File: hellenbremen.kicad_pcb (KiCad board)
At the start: 4 copper layers, 102 x 107 mm, 64 parts, among them IC1 TLE9201SG, J2 Conn_01x03_Pin, J3 USB_C_Receptacle_USB2.0_16P, M1 Module-stlink-0.1, M2 Module-power_12and5V-0.2, M3 Module-mega-mcu144-0.6, M4 Module-vr-max9924-0.1, M5 Module-knock-0.2, M6 Module-knock-0.2, Q1 ISL9V3040D3ST, Q2 ISL9V3040D3ST, Q3 DMN6040SK3-13, Q4 DMN6040SK3-13, U1 RNBD451PE-I100, U2 VNLD5160TR-E, U3 VNLD5160TR-E, U4 VNLD5160TR-E, U7 VNLD5160TR-E, U8 VNLD5160TR-E

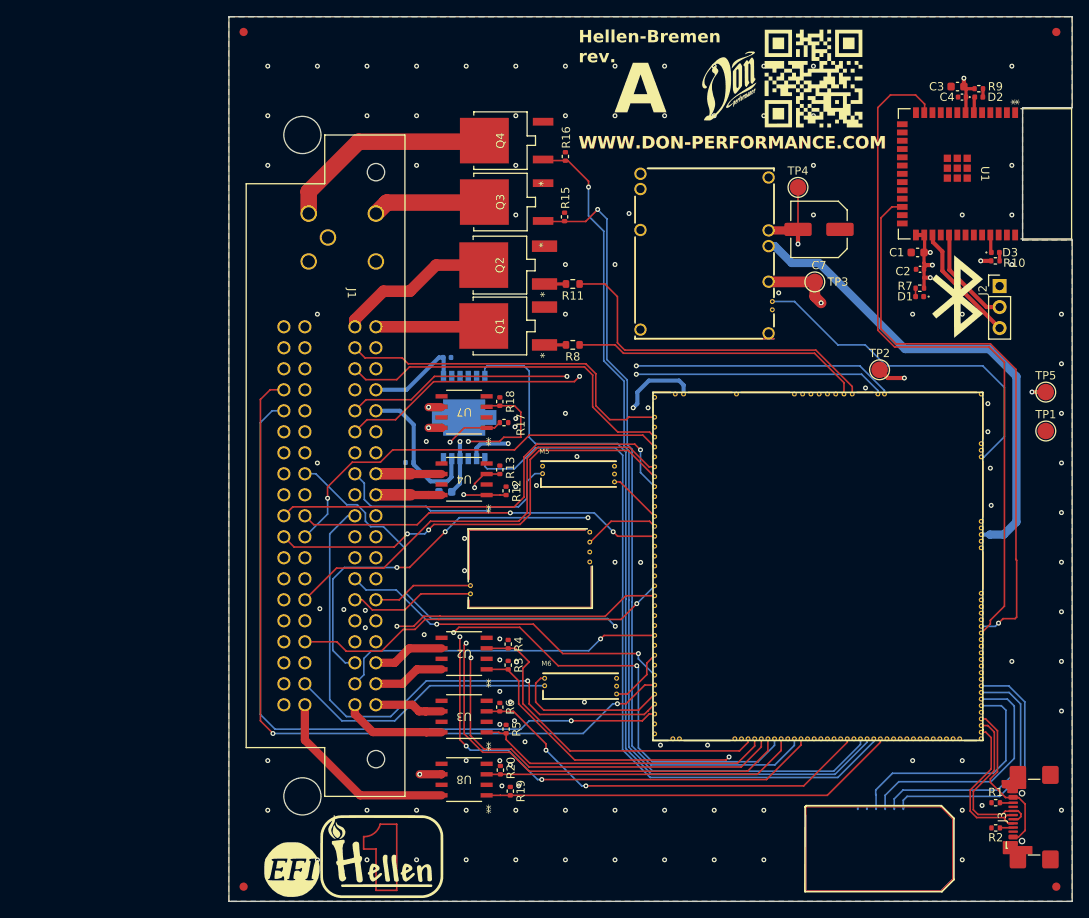
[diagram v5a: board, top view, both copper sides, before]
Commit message: pwm for heaters, minor routing and via changes, teardrops
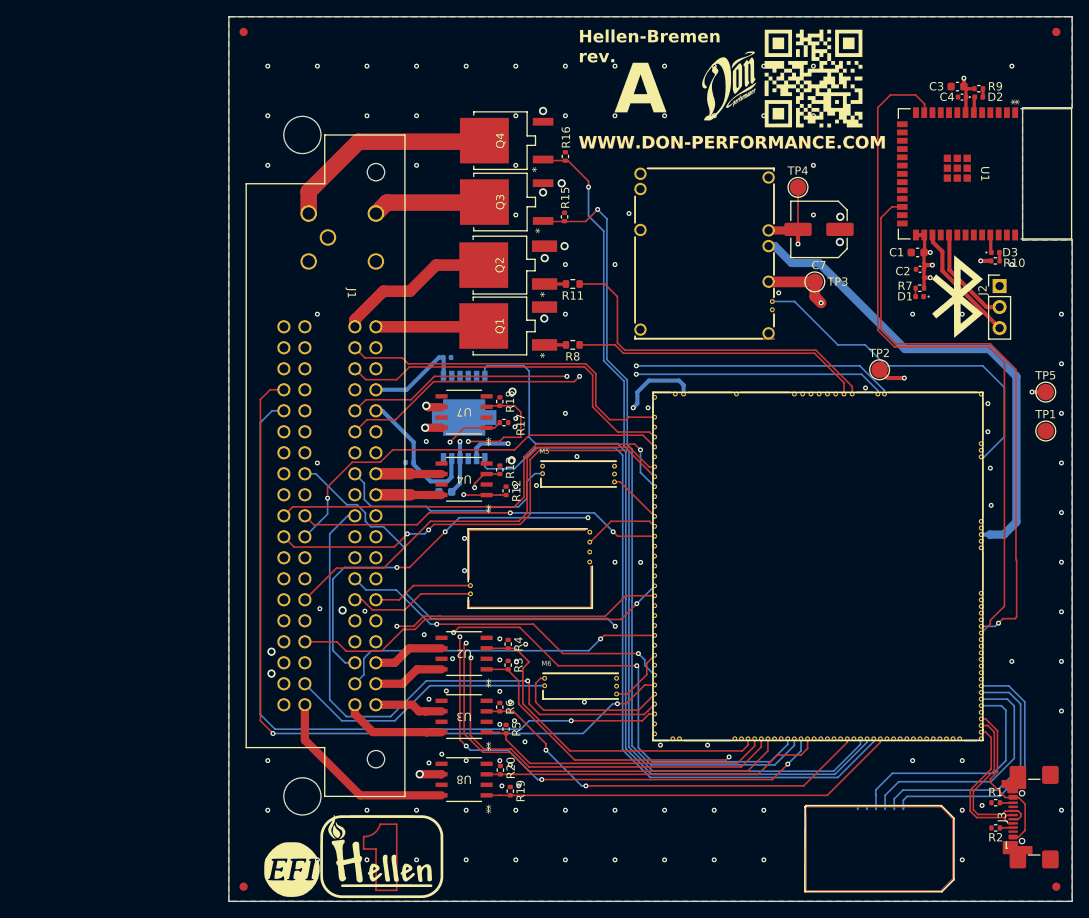
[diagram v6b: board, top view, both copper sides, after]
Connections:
- M3 pad E25: unconnected-(M3-OUT_PWM7-PadE25) -> MCU_FHO2H
- M3 pad E28: unconnected-(M3-OUT_PWM8-PadE28) -> MCU_RHO2H
- M3 pad E29: MCU_FHO2H -> unconnected-(M3-OUT_INJ3-PadE29)
- M3 pad E30: MCU_RHO2H -> unconnected-(M3-OUT_INJ4-PadE30)
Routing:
- net MCU_FHO2H: track 38.2 -> 41.3 mm
- net MCU_RHO2H: track 83.3 -> 84.9 mm
- net ETC_OUT_M: track 18.0 -> 16.8 mm
- net MCU_PCHO2SHTR: track 97.3 -> 97.7 mm, vias 4 -> 5
- net GND: vias 118 -> 132

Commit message: large cap, more silkscreen for big connector
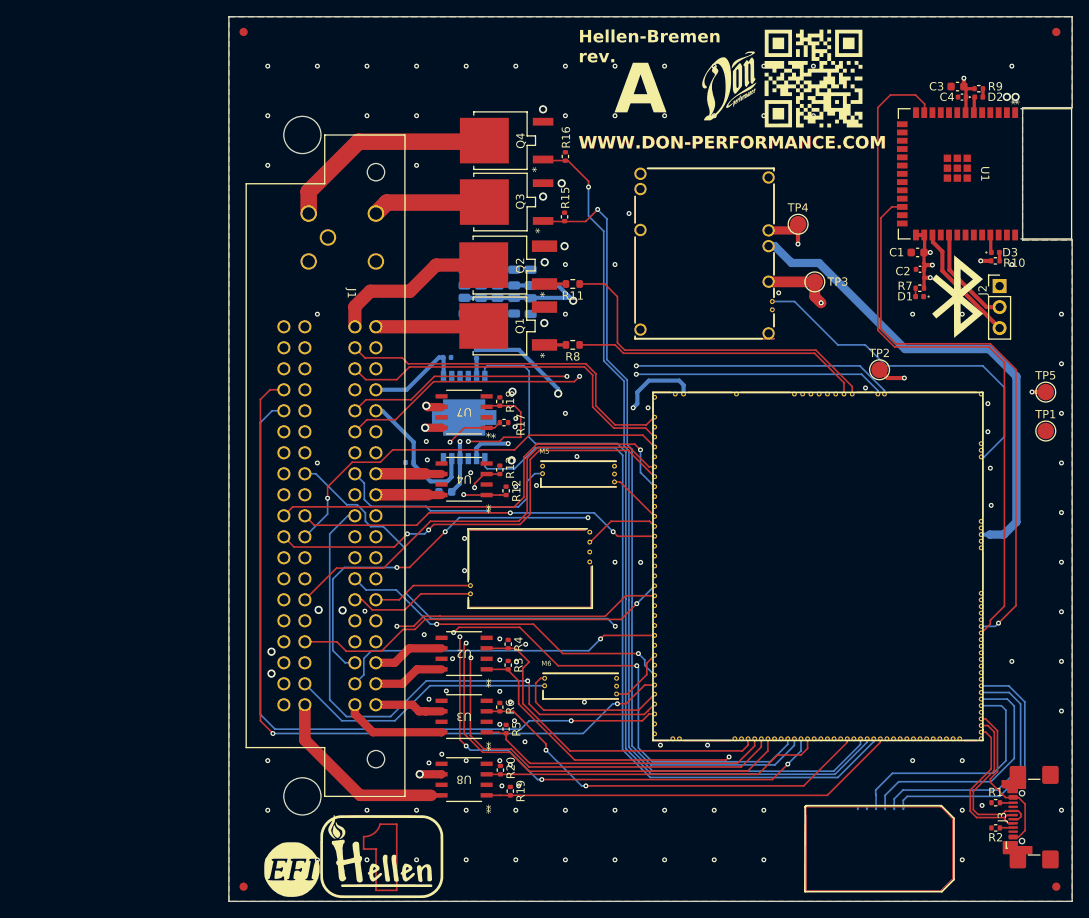
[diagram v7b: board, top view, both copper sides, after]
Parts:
- added ?: , , B.Cu at (97.5, 67.5)
- added C10: 10uF, Capacitor_SMD:C_0805_2012Metric, B.Cu at (95.5, 69.9)
- added C11: 10uF, Capacitor_SMD:C_0805_2012Metric, B.Cu at (93.5, 69.9)
- added C12: 10uF, Capacitor_SMD:C_0805_2012Metric, B.Cu at (91.5, 69.9)
- added C13: 10uF, Capacitor_SMD:C_0805_2012Metric, B.Cu at (89.5, 69.9)
- added C14: 10uF, Capacitor_SMD:C_0805_2012Metric, B.Cu at (91.5, 66.5)
- added C15: 10uF, Capacitor_SMD:C_0805_2012Metric, B.Cu at (93.5, 66.5)
- added C16: 10uF, Capacitor_SMD:C_0805_2012Metric, B.Cu at (97.5, 66.5)
- added C17: 10uF, Capacitor_SMD:C_0805_2012Metric, B.Cu at (97.5, 70.0)
- added C9: 10uF, Capacitor_SMD:C_0805_2012Metric, B.Cu at (89.5, 66.5)
- added R14: R_Small, Resistor_SMD:R_0402_1005Metric, B.Cu at (90.9, 75.8)
- C7: value 100uF -> 10uF; footprint Capacitor_SMD:C_Elec_6.3x5.8 -> Capacitor_SMD:C_0805_2012Metric; moved to B.Cu
- U1: footprint footprints:MOD39_15p5X20p7X2p8_ZSX_MCH -> RNBD451PE:MOD39_15p5X20p7X2p8_ZSX_MCH
- moved C7 37.3 mm to (95.5, 66.5), turned to -90 degrees
- moved TP4 4.46 mm to (129.8, 60.1)
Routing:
- net +12V: track 74.0 -> 102.9 mm, vias 2 -> 3
- net +3V3: track 74.5 -> 86.9 mm, vias 2 -> 3
- net Net-(IC1-DIS): track 0.00 -> 2.19 mm
- net FIVVTC: track 7.96 -> 9.68 mm
- net IGN_2: track 19.2 -> 20.1 mm
- net UART_BT_RX: track 69.7 -> 68.8 mm
- net GND: vias 132 -> 129

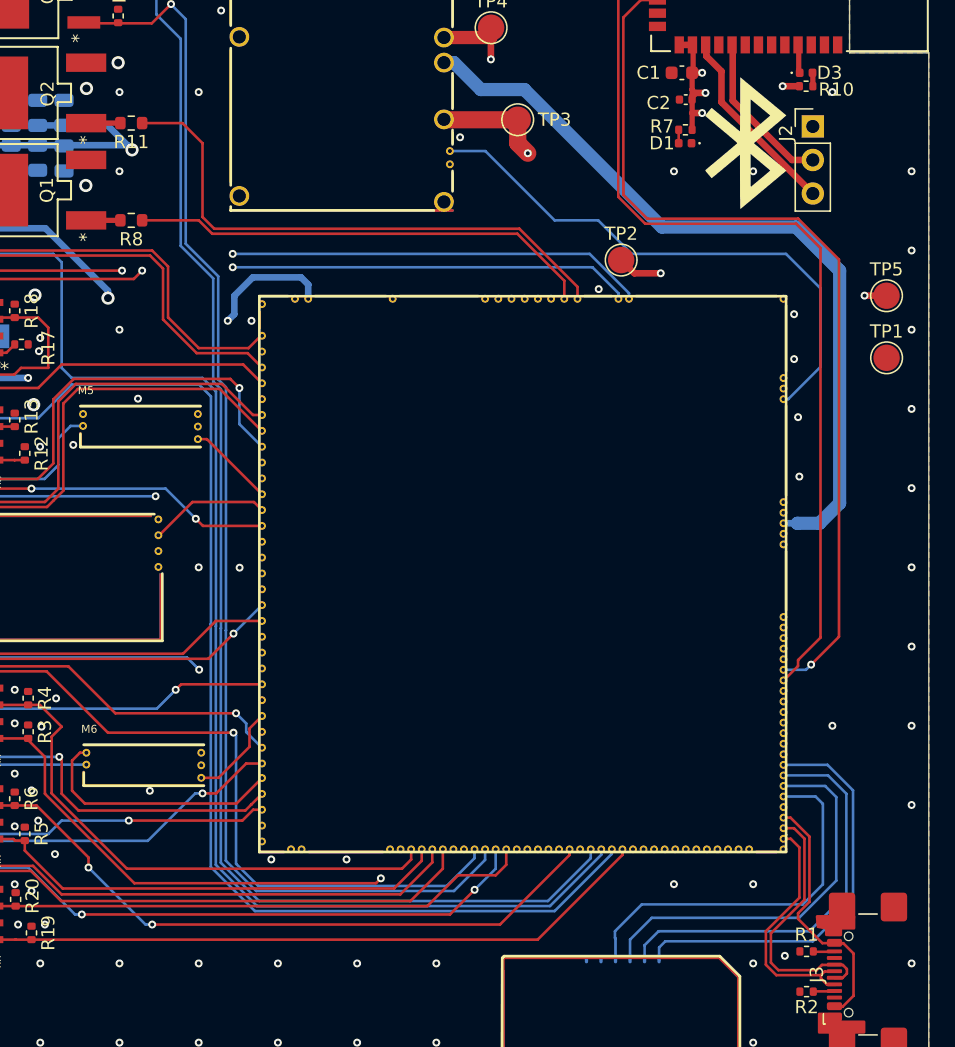
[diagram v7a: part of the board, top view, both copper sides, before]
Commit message: removed unwanted via
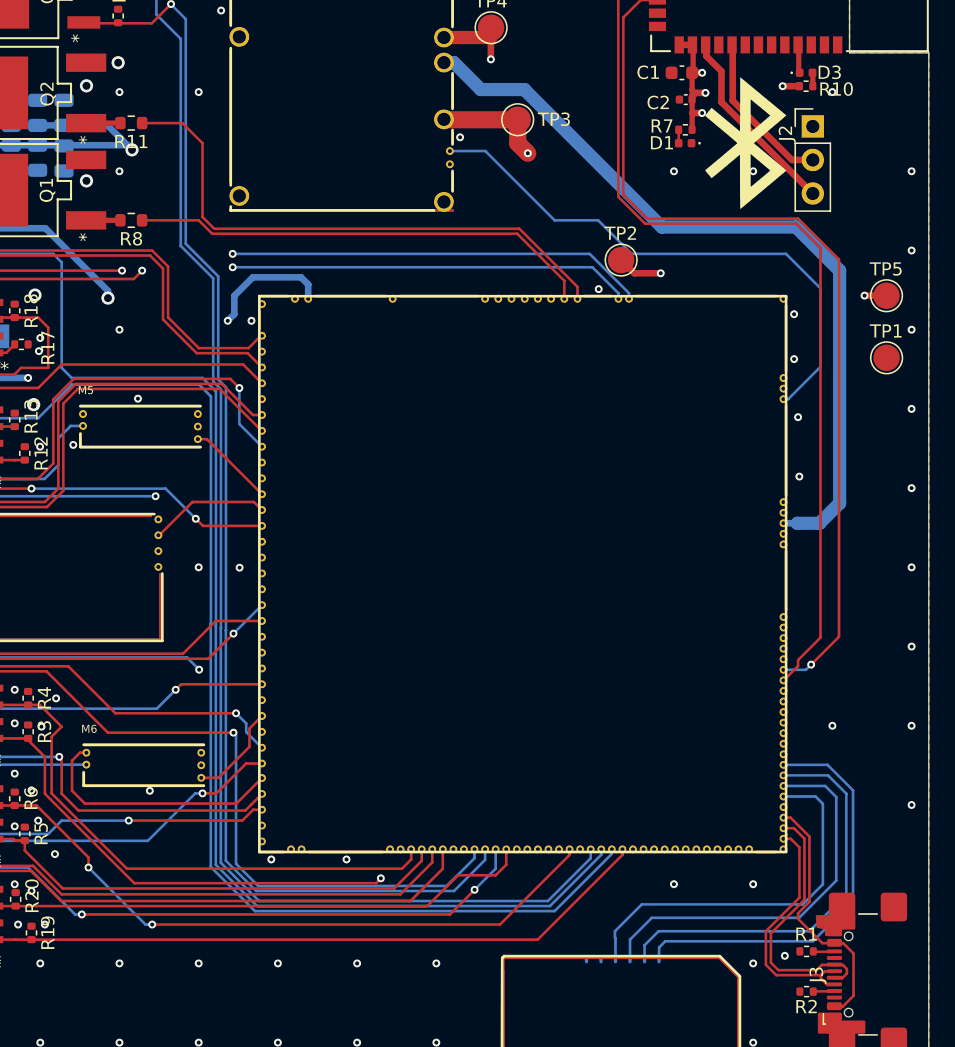
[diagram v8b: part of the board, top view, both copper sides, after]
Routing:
- net GND: vias 129 -> 128
